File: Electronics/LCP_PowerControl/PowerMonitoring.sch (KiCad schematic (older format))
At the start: 18 parts, among them Q2 2N7002, U1 MAX17205

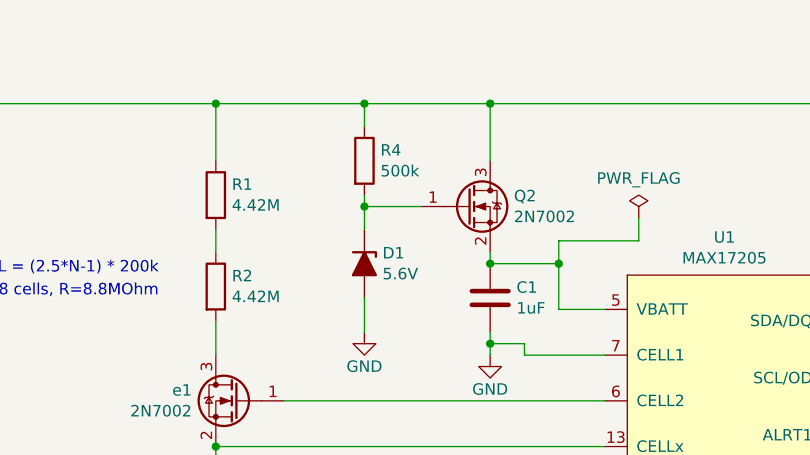
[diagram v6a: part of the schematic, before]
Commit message: BOM Update
Updated MPNs on components to match supplies as well as correcting some resistor values
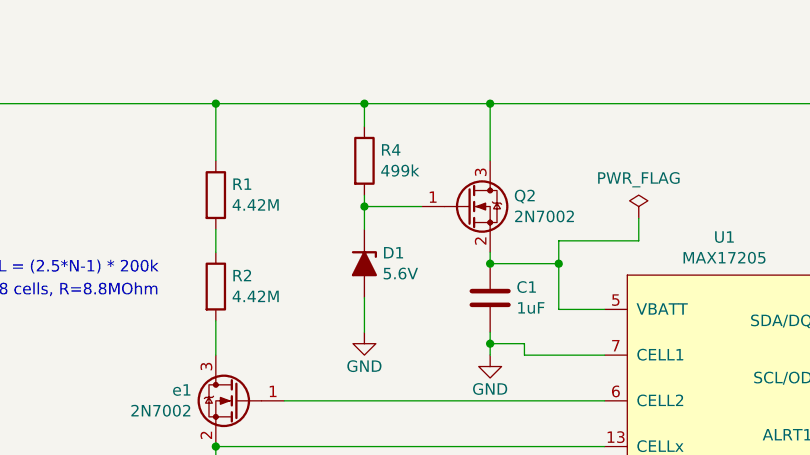
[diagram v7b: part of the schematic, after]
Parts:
- C1: MPN C1206X7R101-105KNE -> CL31B105KCHNNNE
- D1, D2, D3, D4: MPN MM3Z5V6ST1G -> SZMM3Z5V6ST1G
- R1: MPN CRCW08058M87FKEA -> CRCW08054M42FKEA
- R4: value 500k -> 499k; MPN CRCW08058M87FKEA -> RC0805FR-07499KL
- U1: MPN (none) -> MAX17205G+T
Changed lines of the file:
@@
 F 2 "Package_DFN_QFN:DFN-14-1EP_3x3mm_P0.4mm_EP1.78x2.35mm" H 6150 2950 50  0001 C CNN
 F 3 "https://datasheets.maximintegrated.com/en/ds/MAX17201-MAX17215.pdf" H 5600 4350 50  0001 C CNN
+F 4 "MAX17205G+T" H 5950 3700 50  0001 C CNN "MPN"
 	1    5950 3700
 	1    0    0    -1
@@
 F 2 "Diode_SMD:D_SOD-323_HandSoldering" H 7950 4000 50  0001 C CNN
 F 3 "~" H 7950 4000 50  0001 C CNN
-F 4 "MM3Z5V6ST1G" V 7950 4000 50  0001 C CNN "MPN"
+F 4 "SZMM3Z5V6ST1G" V 7950 4000 50  0001 C CNN "MPN"
 	1    7950 4000
 	0    1    1    0
@@
 F 2 "Diode_SMD:D_SOD-323_HandSoldering" H 7650 4000 50  0001 C CNN
 F 3 "~" H 7650 4000 50  0001 C CNN
-F 4 "MM3Z5V6ST1G" V 7650 4000 50  0001 C CNN "MPN"
+F 4 "SZMM3Z5V6ST1G" V 7650 4000 50  0001 C CNN "MPN"
 	1    7650 4000
 	0    1    1    0
@@
 F 2 "Diode_SMD:D_SOD-323_HandSoldering" H 8250 4000 50  0001 C CNN
 F 3 "~" H 8250 4000 50  0001 C CNN
-F 4 "MM3Z5V6ST1G" V 8250 4000 50  0001 C CNN "MPN"
+F 4 "SZMM3Z5V6ST1G" V 8250 4000 50  0001 C CNN "MPN"
 	1    8250 4000
 	0    1    1    0
@@
 F 2 "Resistor_SMD:R_0805_2012Metric" V 3630 2700 50  0001 C CNN
 F 3 "~" H 3700 2700 50  0001 C CNN
-F 4 "CRCW08058M87FKEA" H 3700 2700 50  0001 C CNN "MPN"
+F 4 "CRCW08054M42FKEA" H 3700 2700 50  0001 C CNN "MPN"
 	1    3700 2700
 	1    0    0    -1
@@
 F 2 "Diode_SMD:D_SOD-323_HandSoldering" H 4350 3000 50  0001 C CNN
 F 3 "~" H 4350 3000 50  0001 C CNN
-F 4 "MM3Z5V6ST1G" V 4350 3000 50  0001 C CNN "MPN"
+F 4 "SZMM3Z5V6ST1G" V 4350 3000 50  0001 C CNN "MPN"
 	1    4350 3000
 	0    1    1    0
@@
 F 2 "Capacitor_SMD:C_0805_2012Metric" H 4938 3000 50  0001 C CNN
 F 3 "~" H 4900 3150 50  0001 C CNN
-F 4 "C1206X7R101-105KNE" H 4900 3150 50  0001 C CNN "MPN"
+F 4 "CL31B105KCHNNNE" H 4900 3150 50  0001 C CNN "MPN"
 	1    4900 3150
 	1    0    0    -1
@@
 Wire Wire Line
 	5700 4850 5700 5300
+Wire Wire Line
+	8900 3750 10350 3750
+Wire Wire Line
+	8900 3500 10350 3500
+Wire Wire Line
+	8900 3250 10350 3250
+Wire Wire Line
+	1650 5300 5700 5300
+Wire Wire Line
+	4900 2300 7450 2300
 $Comp
 L Device:R R4
@@
 P 4350 2550
 F 0 "R4" H 4420 2596 50  0000 L CNN
-F 1 "500k" H 4420 2505 50  0000 L CNN
+F 1 "499k" H 4420 2505 50  0000 L CNN
 F 2 "Resistor_SMD:R_0805_2012Metric" V 4280 2550 50  0001 C CNN
 F 3 "~" H 4350 2550 50  0001 C CNN
-F 4 "CRCW08058M87FKEA" H 4350 2550 50  0001 C CNN "MPN"
+F 4 "RC0805FR-07499KL" H 4350 2550 50  0001 C CNN "MPN"
 	1    4350 2550
 	1    0    0    -1
 $EndComp
-Wire Wire Line
-	8900 3750 10350 3750
-Wire Wire Line
-	8900 3500 10350 3500
-Wire Wire Line
-	8900 3250 10350 3250
-Wire Wire Line
-	1650 5300 5700 5300
-Wire Wire Line
-	4900 2300 7450 2300
 $EndSCHEMATC

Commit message: adding power control to pull-ups.
Adding ability to power on/off the pull-ups on the encoder
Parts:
- U1: symbol LCP_PowerControl-rescue:MAX17205-PMEL_BatteryManagement-LCP_PowerControl-rescue -> LCP_PowerControl-rescue:MAX17205-PMEL_BatteryManagement-LCP_PowerControl-rescue-LCP_PowerControl-rescue
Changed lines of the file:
@@
 $EndDescr
 $Comp
-L LCP_PowerControl-rescue:MAX17205-PMEL_BatteryManagement-LCP_PowerControl-rescue U1
+L LCP_PowerControl-rescue:MAX17205-PMEL_BatteryManagement-LCP_PowerControl-rescue-LCP_PowerControl-rescue U1
 U 1 1 5EE2E9B5
 P 5950 3700
